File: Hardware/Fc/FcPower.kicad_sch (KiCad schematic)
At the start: 27 parts, among them J1 PWR, U2 INA219AIDCNR

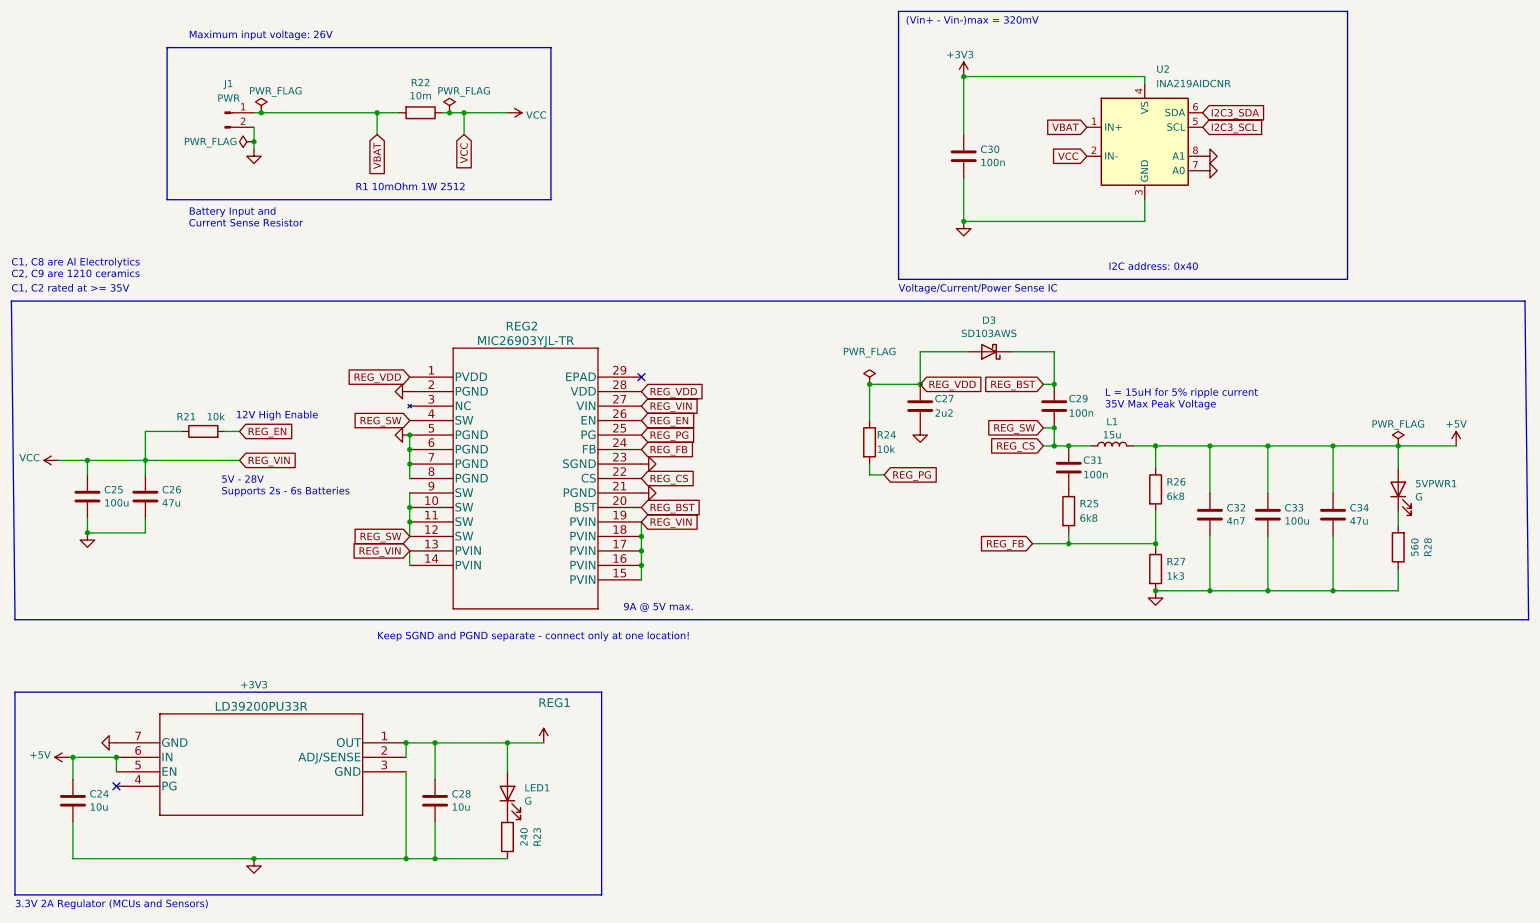
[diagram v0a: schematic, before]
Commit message: Added USB
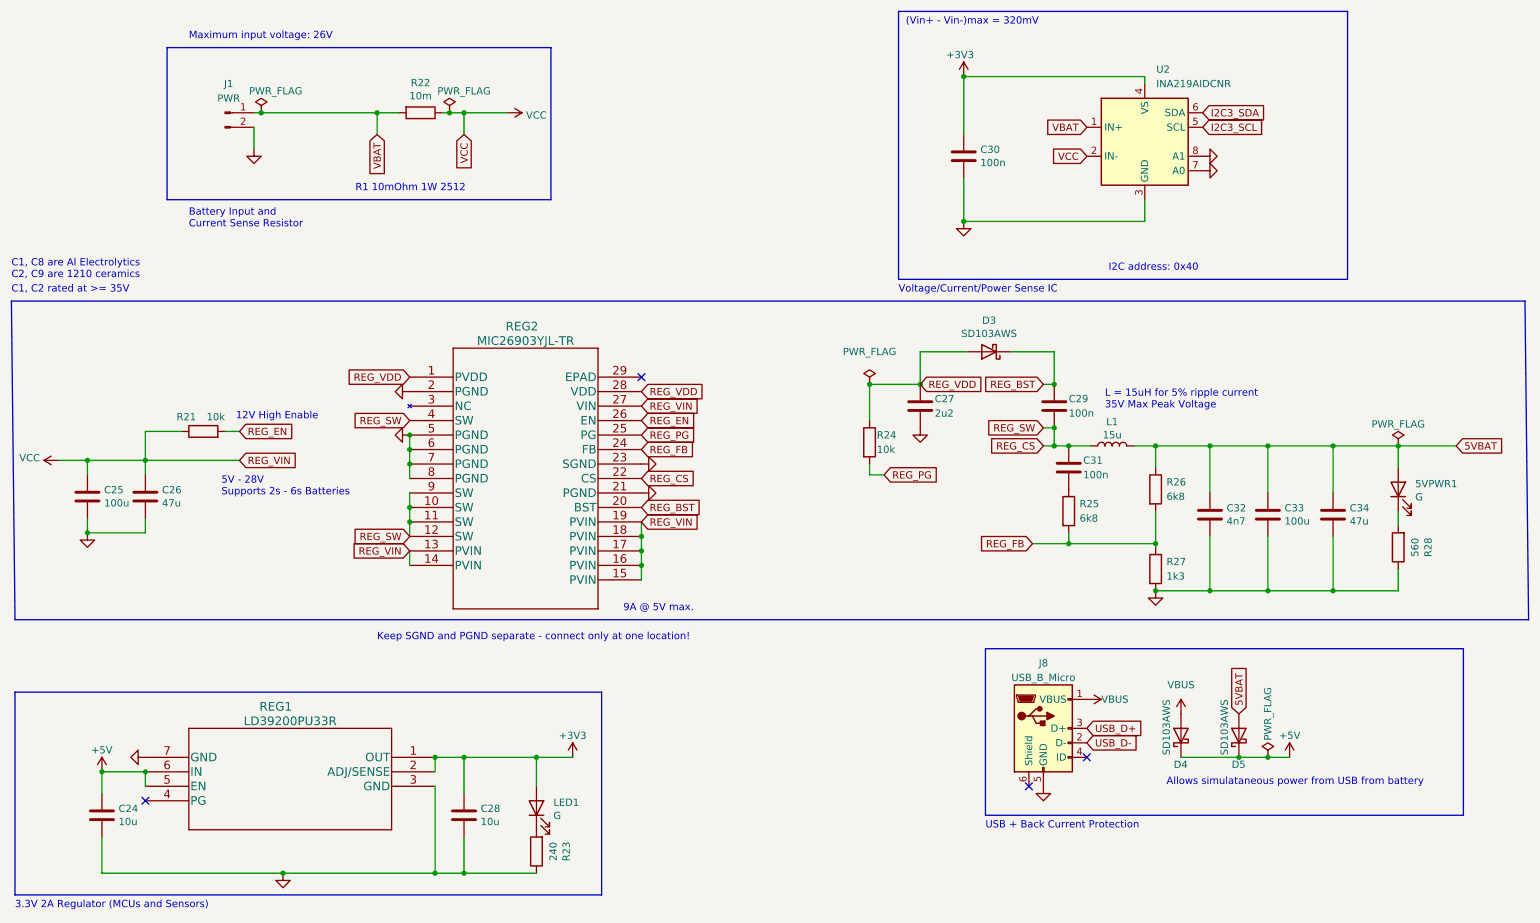
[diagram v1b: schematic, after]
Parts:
- added D4, D5: SD103AWS, symbol Device:D_Schottky
- added J8: USB_B_Micro, symbol Connector:USB_B_Micro
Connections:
- net +5V: now also D4.1 (K), D5.1 (K); no longer 5VPWR1.2 (A), C32.1, C33.1, C34.1, L1.2, R26.1
- net GND: now also J8.5 (GND)
- new net 5VBAT: 5VPWR1.2 (A), C32.1, C33.1, C34.1, D5.2 (A), L1.2, R26.1
- new net USB_D+: J8.3 (D+)
- new net USB_D-: J8.2 (D-)
- new net VBUS: D4.2 (A), J8.1 (VBUS)
- no-connect marks 2 -> 4
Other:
- note added: "Allows simulataneous power from USB from battery"
- note added: "USB + Back Current Protection"
- moved on the sheet: C24, C28, LED1, R23, REG1

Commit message: Building with new libcamera updates
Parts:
- D4, D5: footprint (none) -> Diode_SMD:D_SOD-323
- J8: footprint (none) -> Connector_USB:USB_Micro-B_Wuerth_629105150521
- L1: footprint cad:SRP1265A-470M -> Inductor_SMD:L_Bourns_SRP1245A
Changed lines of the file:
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@@
     (property "Reference" "J8" (id 0) (at 196.85 133.35 0))
     (property "Value" "USB_B_Micro" (id 1) (at 196.85 135.89 0))
-    (property "Footprint" "" (id 2) (at 200.66 146.05 0)
+    (property "Footprint" "Connector_USB:USB_Micro-B_Wuerth_629105150521" (id 2) (at 200.66 146.05 0)
       (effects (font (size 1.27 1.27)) hide)
     )
@@
     (property "Reference" "L1" (id 0) (at 208.915 91.0336 90))
     (property "Value" "15u" (id 1) (at 208.915 93.345 90))
-    (property "Footprint" "cad:SRP1265A-470M" (id 2) (at 208.915 95.25 0)
+    (property "Footprint" "Inductor_SMD:L_Bourns_SRP1245A" (id 2) (at 208.915 95.25 0)
       (effects (font (size 1.27 1.27)) hide)
     )
@@
       (effects (font (size 1.27 1.27)) (justify right))
     )
-    (property "Footprint" "" (id 2) (at 220.98 146.05 0)
+    (property "Footprint" "Diode_SMD:D_SOD-323" (id 2) (at 220.98 146.05 0)
       (effects (font (size 1.27 1.27)) hide)
     )
@@
       (effects (font (size 1.27 1.27)) (justify right))
     )
-    (property "Footprint" "" (id 2) (at 231.14 146.05 0)
-      (effects (font (size 1.27 1.27)) hide)
-    )
+    (property "Footprint" "Diode_SMD:D_SOD-323" (id 2) (at 231.14 146.05 0)
+      (effects (font (size 1.27 1.27)) hide)
+    )
